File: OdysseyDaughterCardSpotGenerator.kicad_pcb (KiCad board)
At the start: 2 copper layers, 37.1 x 46.6 mm, 22 parts, among them J1 Conn_01x03, J2 Conn_01x02, Q1 2N3904, Q2 2N3904, Q3 BC547C, Q4 2N3904, X1 OdysseyDaughterCard

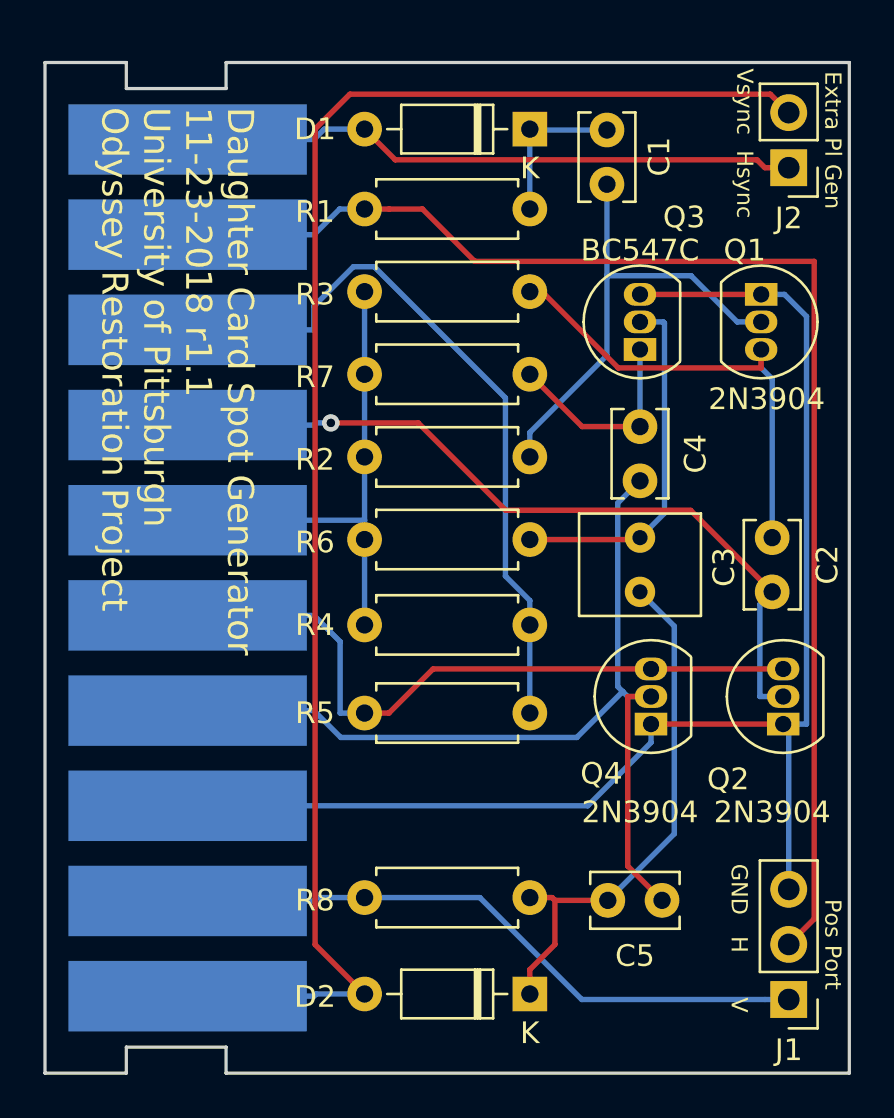
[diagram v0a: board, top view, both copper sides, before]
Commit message: Add gnd and vdd to extra player interface port still R1.2
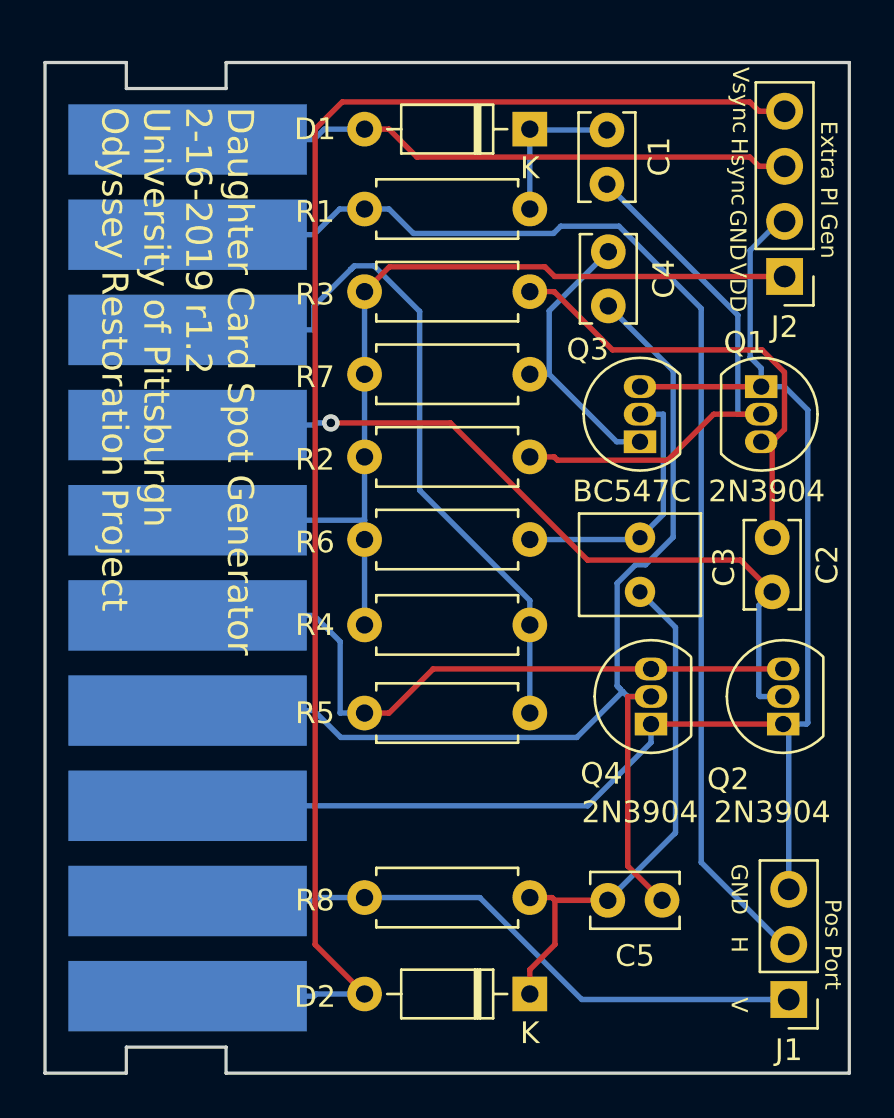
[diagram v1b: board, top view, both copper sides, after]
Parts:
- J2: value Conn_01x02 -> Conn_01x04; footprint Connector_PinHeader_2.54mm:PinHeader_1x02_P2.54mm_Vertical -> Connector_PinHeader_2.54mm:PinHeader_1x04_P2.54mm_Vertical
- moved C4 8.20 mm to (148.4, 86.4)
- moved J2 5.02 mm to (156.5, 87.6)
- moved Q1 4.25 mm to (155.4, 92.6)
- moved Q3 4.25 mm to (149.9, 95.2)
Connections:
- J2 pad 1: /Card10 -> /Card6
- J2 pad 2: /Card1 -> GND
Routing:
- net /Card6: track 23.5 -> 43.6 mm
- net /Card4: track 44.2 -> 54.6 mm
- net /Card9: track 62.4 -> 57.9 mm
- net GND: track 65.2 -> 69.7 mm
- net Net-(C3-Pad2): track 16.6 -> 12.3 mm
- net Net-(C1-Pad1): track 22.0 -> 25.8 mm
- net Net-(C4-Pad1): track 9.64 -> 13.1 mm
- net /Card1: track 71.9 -> 71.4 mm
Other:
- board text added: "Daughter Card Spot Generator 2-16-2019 r1.2 University of Pittsburgh Odyssey Restoration Project"
- board text added: "VDD"
- board text removed: "Daughter Card Spot Generator 11-23-2018 r1.1 University of Pittsburgh Odyssey Restoration Project"
